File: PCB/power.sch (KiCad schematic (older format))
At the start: 45 parts

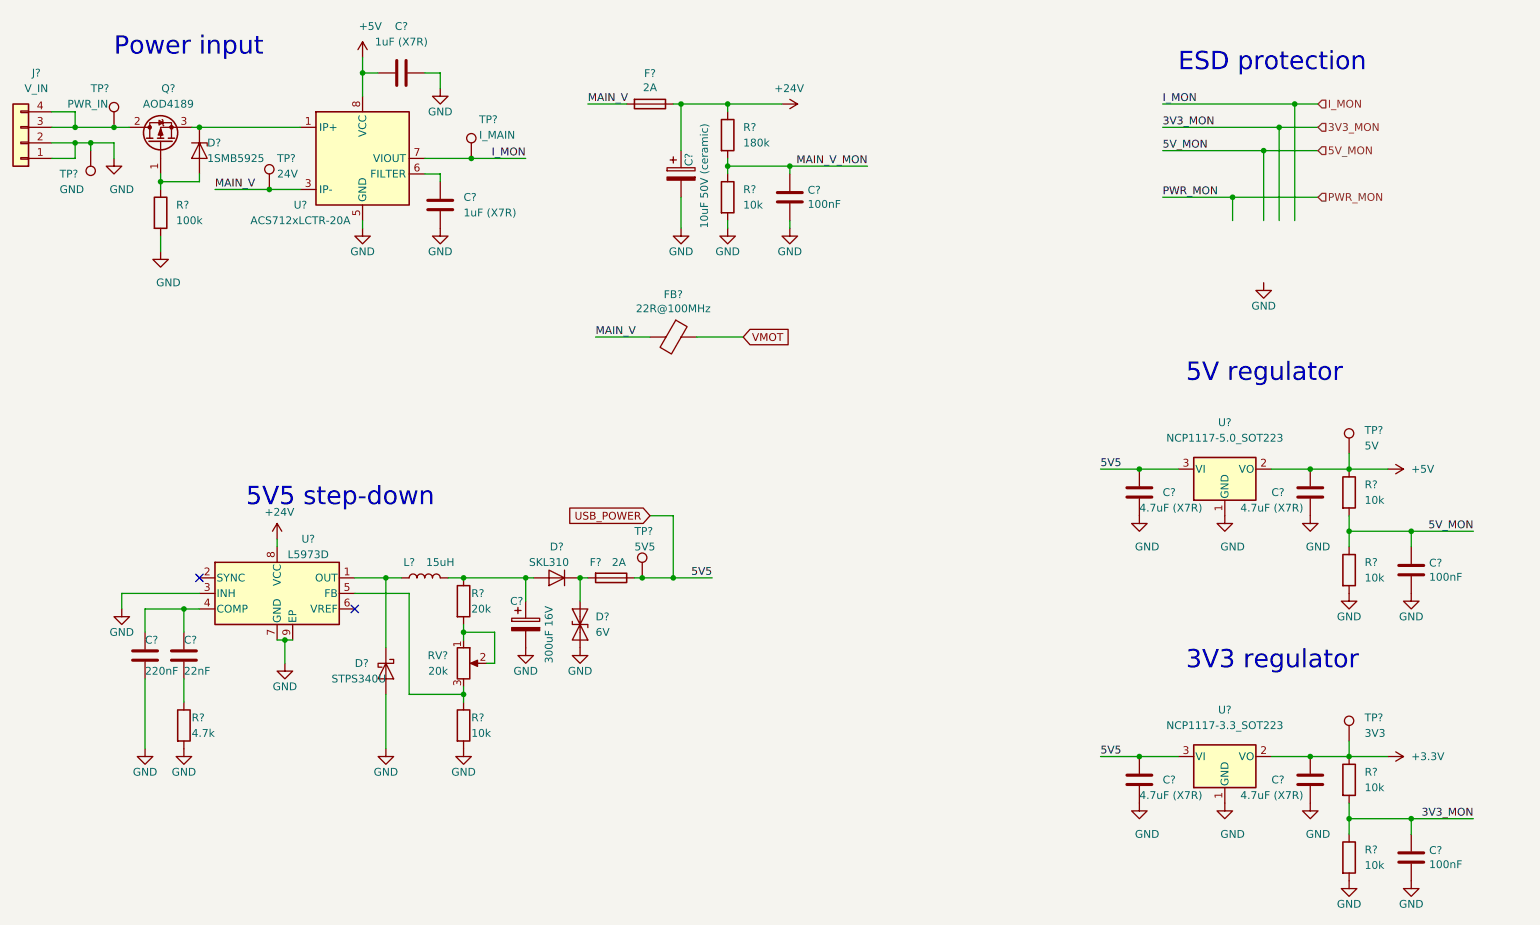
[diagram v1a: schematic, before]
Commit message: Schema: add Interface schema, remove old mcu, add divider to current measuring
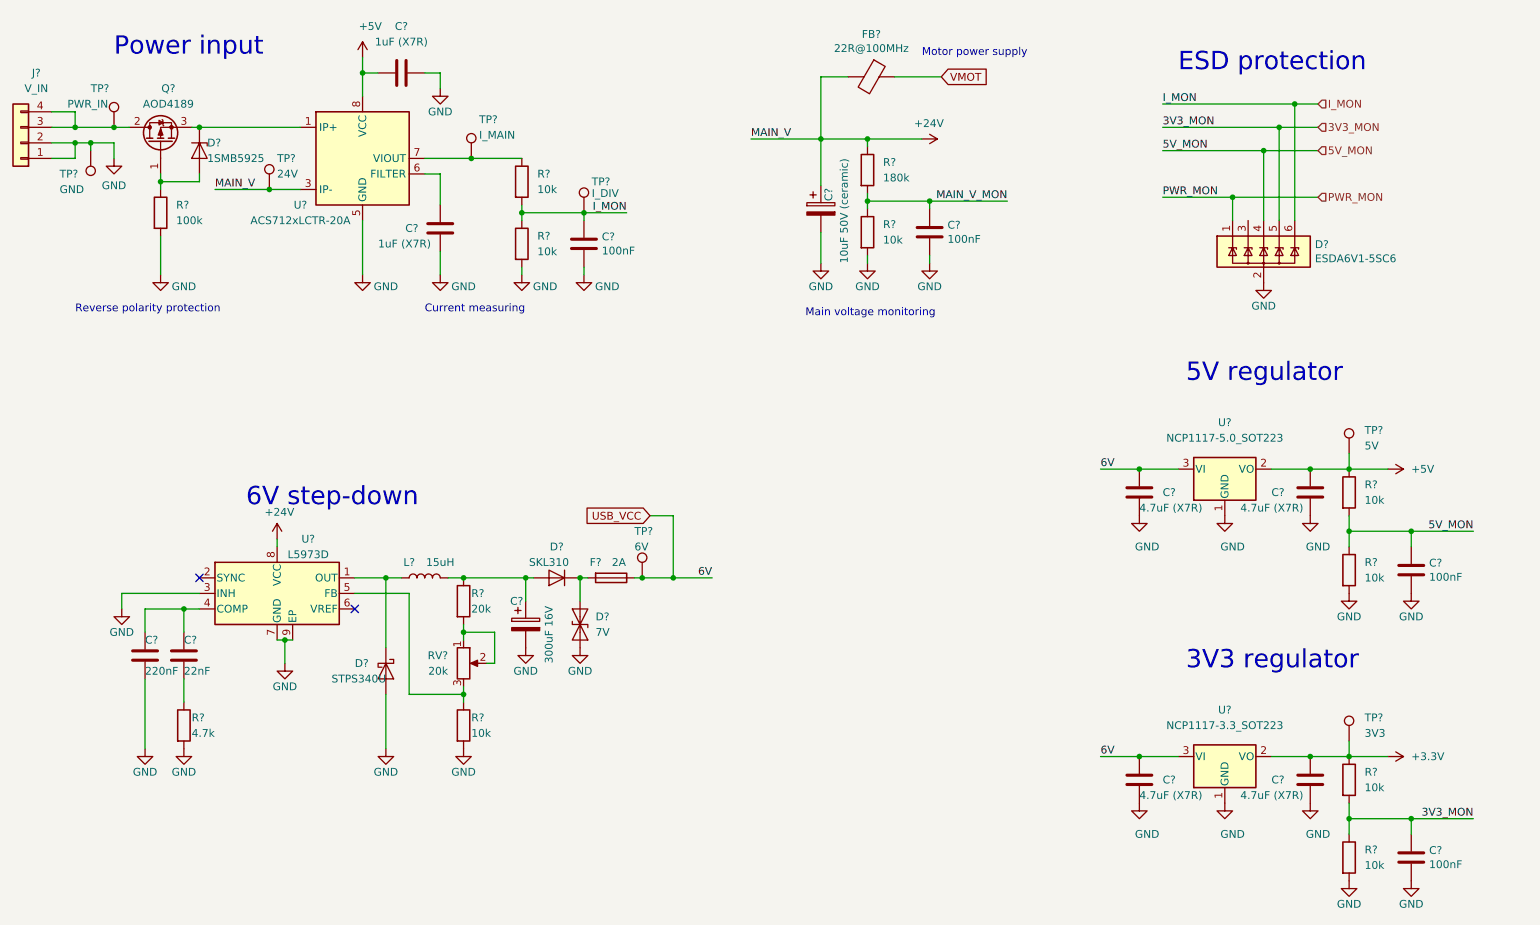
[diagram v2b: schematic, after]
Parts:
- removed F?: 2A, symbol Device:Fuse
- added C?: 100nF, Capacitor_SMD:C_0603_1608Metric, symbol Device:C
- added D?: ESDA6V1-5SC6, Package_TO_SOT_SMD:SOT-23-6, symbol Power_Protection:ESDA6V1-5SC6
- added R? (x2): 10k, Resistor_SMD:R_0603_1608Metric, symbol Device:R
- added TP?: I_DIV, symbol Connector:TestPoint
- D?: value 6V -> 7V
- TP?: value 5V5 -> 6V
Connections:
- net labels added: 6V, USB_VCC
- net labels removed: 5V5, USB_POWER
- wire segments 118 -> 126
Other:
- note added: "6V step-down"
- note added: "Current measuring"
- note added: "Main voltage monitoring"
- note added: "Motor power supply"
- note added: "Reverse polarity protection"
- note removed: "5V5 step-down"
- moved on the sheet: C?, FB?, R?

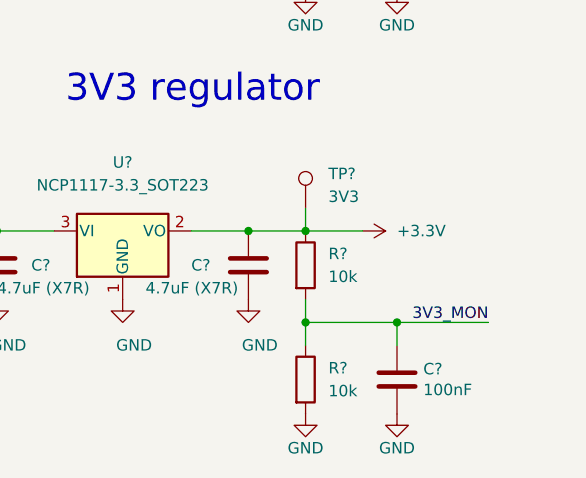
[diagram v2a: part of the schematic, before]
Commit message: Schema: add mcu, RGB LED signalization, reset circuit
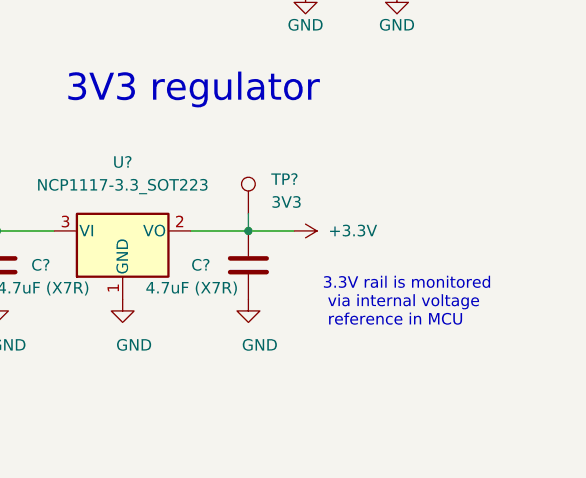
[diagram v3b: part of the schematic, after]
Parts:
- removed C?: 100nF, Capacitor_SMD:C_0603_1608Metric, symbol Device:C
- removed R? (x2): 10k, Resistor_SMD:R_0603_1608Metric, symbol Device:R
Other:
- note added: "3.3V rail is monitored\n via internal voltage\n reference in MCU"
- moved on the sheet: TP?
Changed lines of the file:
@@
-$EndComp
-$Comp
-L Device:R R?
-U 1 1 5CE09E51
-P 9650 5500
-F 0 "R?" H 9750 5550 50  0000 L CNN
-F 1 "10k" H 9750 5450 50  0000 L CNN
-F 2 "Resistor_SMD:R_0603_1608Metric" V 9580 5500 50  0001 C CNN
-F 3 "~" H 9650 5500 50  0001 C CNN
-	1    9650 5500
-	1    0    0    -1
-$EndComp
-$Comp
-L Device:R R?
-U 1 1 5CE09E5B
-P 9650 6000
-F 0 "R?" H 9750 6050 50  0000 L CNN
-F 1 "10k" H 9750 5950 50  0000 L CNN
-F 2 "Resistor_SMD:R_0603_1608Metric" V 9580 6000 50  0001 C CNN
-F 3 "~" H 9650 6000 50  0001 C CNN
-	1    9650 6000
-	1    0    0    -1
-$EndComp
-$Comp
-L power:GND #PWR?
-U 1 1 5CE09E69
-P 9650 6150
-F 0 "#PWR?" H 9650 5900 50  0001 C CNN
-F 1 "GND" H 9650 6000 50  0000 C CNN
-F 2 "" H 9650 6150 50  0001 C CNN
-F 3 "" H 9650 6150 50  0001 C CNN
-	1    9650 6150
-	1    0    0    -1
 $EndComp
 $Comp
 L power:+3.3V #PWR?
 U 1 1 5CE30936
-P 9900 5350
-F 0 "#PWR?" H 9900 5200 50  0001 C CNN
-F 1 "+3.3V" V 9900 5500 50  0000 L CNN
-F 2 "" H 9900 5350 50  0001 C CNN
-F 3 "" H 9900 5350 50  0001 C CNN
-	1    9900 5350
+P 9600 5350
+F 0 "#PWR?" H 9600 5200 50  0001 C CNN
+F 1 "+3.3V" V 9600 5500 50  0000 L CNN
+F 2 "" H 9600 5350 50  0001 C CNN
+F 3 "" H 9600 5350 50  0001 C CNN
+	1    9600 5350
 	0    1    1    0
 $EndComp
-Wire Wire Line
-	9650 5350 9900 5350
 $Comp
 L Device:R R?
@@
 Wire Wire Line
 	9650 3500 9900 3500
-Wire Wire Line
-	9650 5350 9400 5350
-Connection ~ 9650 5350
 Connection ~ 9400 5350
 Wire Wire Line
@@
 L Connector:TestPoint TP?
 U 1 1 5CFEFE42
-P 9650 5250
-F 0 "TP?" H 9750 5400 50  0000 L CNN
-F 1 "3V3" H 9750 5300 50  0000 L CNN
-F 2 "TestPoint:TestPoint_THTPad_D1.5mm_Drill0.7mm" H 9850 5250 50  0001 C CNN
-F 3 "~" H 9850 5250 50  0001 C CNN
-	1    9650 5250
-	1    0    0    -1
-$EndComp
-Wire Wire Line
-	9650 5250 9650 5350
+P 9400 5275
+F 0 "TP?" H 9500 5425 50  0000 L CNN
+F 1 "3V3" H 9500 5325 50  0000 L CNN
+F 2 "TestPoint:TestPoint_THTPad_D1.5mm_Drill0.7mm" H 9600 5275 50  0001 C CNN
+F 3 "~" H 9600 5275 50  0001 C CNN
+	1    9400 5275
+	1    0    0    -1
+$EndComp
 Wire Wire Line
 	5100 4200 5300 4200
@@
 	9200 1300 8450 1300
 Connection ~ 9200 1300
-Wire Wire Line
-	9650 5650 9650 5750
-$Comp
-L Device:C C?
-U 1 1 5D11DA30
-P 10050 6000
-F 0 "C?" H 10165 6046 50  0000 L CNN
-F 1 "100nF" H 10165 5955 50  0000 L CNN
-F 2 "Capacitor_SMD:C_0603_1608Metric" H 10088 5850 50  0001 C CNN
-F 3 "~" H 10050 6000 50  0001 C CNN
-	1    10050 6000
-	1    0    0    -1
-$EndComp
-$Comp
-L power:GND #PWR?
-U 1 1 5D11DA3A
-P 10050 6150
-F 0 "#PWR?" H 10050 5900 50  0001 C CNN
-F 1 "GND" H 10050 6000 50  0000 C CNN
-F 2 "" H 10050 6150 50  0001 C CNN
-F 3 "" H 10050 6150 50  0001 C CNN
-	1    10050 6150
-	1    0    0    -1
-$EndComp
-Wire Wire Line
-	9650 5750 10050 5750
-Connection ~ 10050 5750
-Text Label 10450 5750 2    50   ~ 0
-3V3_MON
-Wire Wire Line
-	10050 5750 10450 5750
-Wire Wire Line
-	10050 5750 10050 5850
-Connection ~ 9650 5750
-Wire Wire Line
-	9650 5750 9650 5850
 Text Label 8450 1300 0    50   ~ 0
 3V3_MON
@@
 Wire Wire Line
 	4325 1850 4725 1850
+Wire Wire Line
+	9400 5275 9400 5350
+Wire Wire Line
+	9400 5350 9600 5350
+Text Notes 9725 5775 0    50   ~ 0
+3.3V rail is monitored\n via internal voltage\n reference in MCU
 $EndSCHEMATC

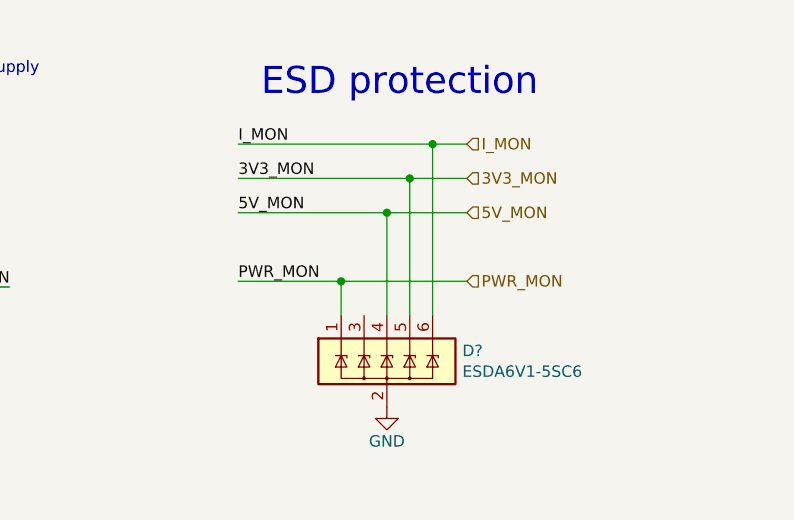
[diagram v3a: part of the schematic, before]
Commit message: Schema: add FLAG and BUSY LED signalization, fix driver ground connection
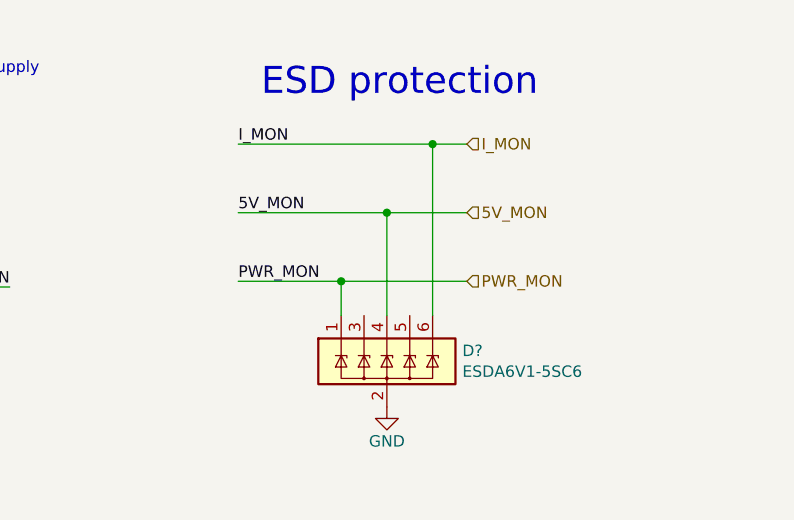
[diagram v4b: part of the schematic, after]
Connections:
- net 3V3_MON: no longer names the net of D?.5 (IO4)
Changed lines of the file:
@@
 Text HLabel 9450 1450 2    50   Input ~ 0
 5V_MON
-Text HLabel 9450 1300 2    50   Input ~ 0
-3V3_MON
 Text HLabel 9450 1750 2    50   Input ~ 0
 PWR_MON
@@
 	9100 1450 9450 1450
 Wire Wire Line
-	9200 1900 9200 1300
-Wire Wire Line
-	9200 1300 9450 1300
-Wire Wire Line
 	8450 1450 9100 1450
 Connection ~ 9100 1450
-Wire Wire Line
-	9200 1300 8450 1300
-Connection ~ 9200 1300
-Text Label 8450 1300 0    50   ~ 0
-3V3_MON
 Text Label 8450 1450 0    50   ~ 0
 5V_MON

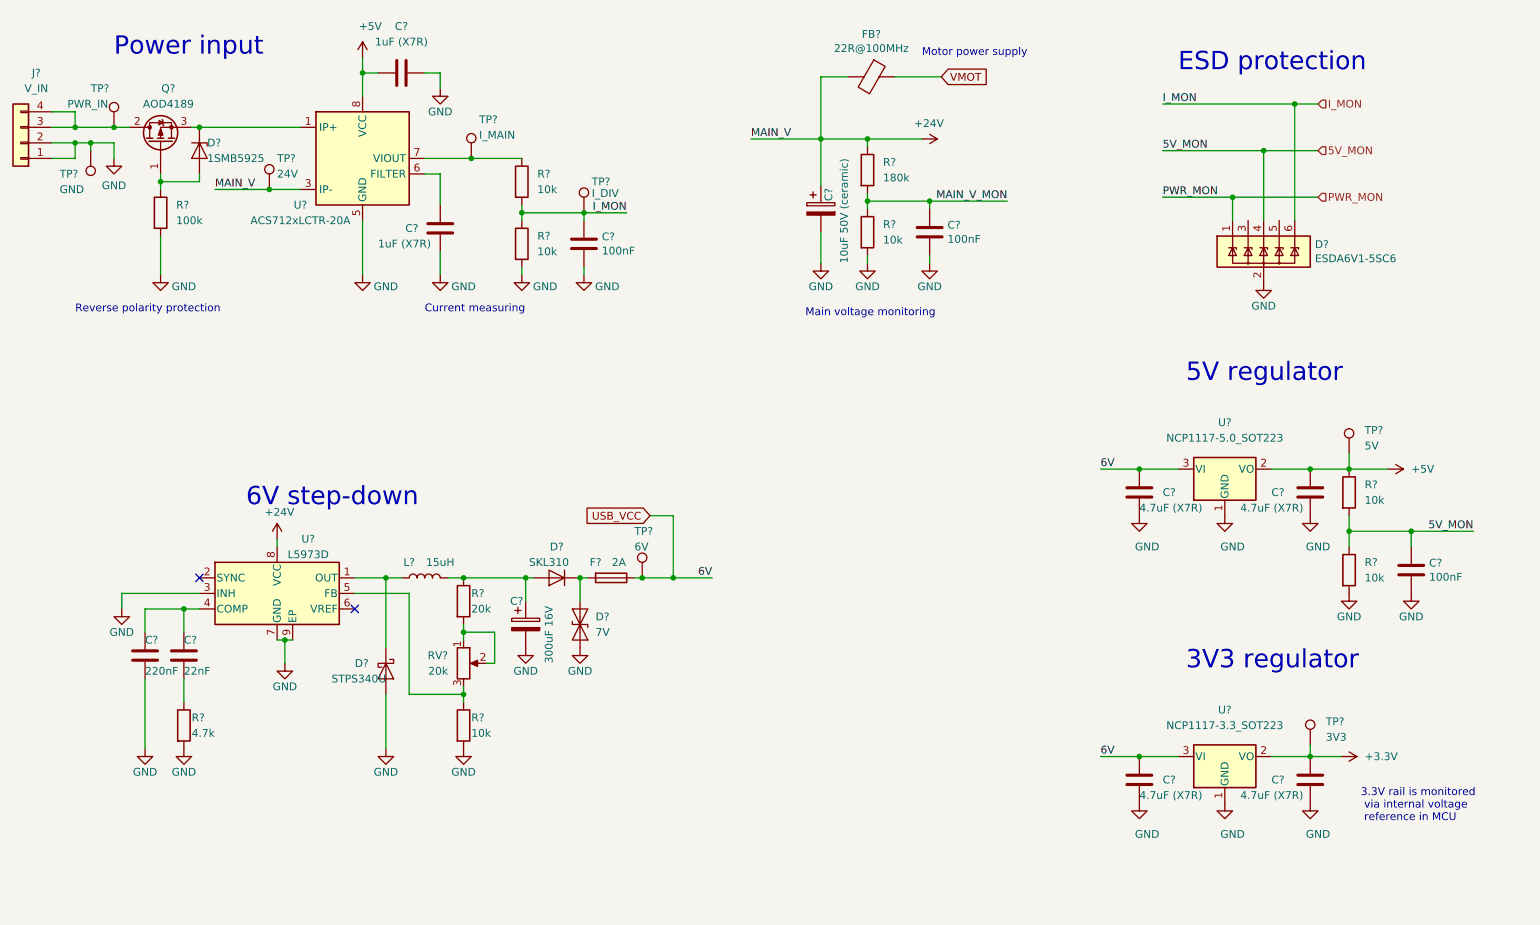
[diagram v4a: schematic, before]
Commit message: Schema: new part annotation, package assignment
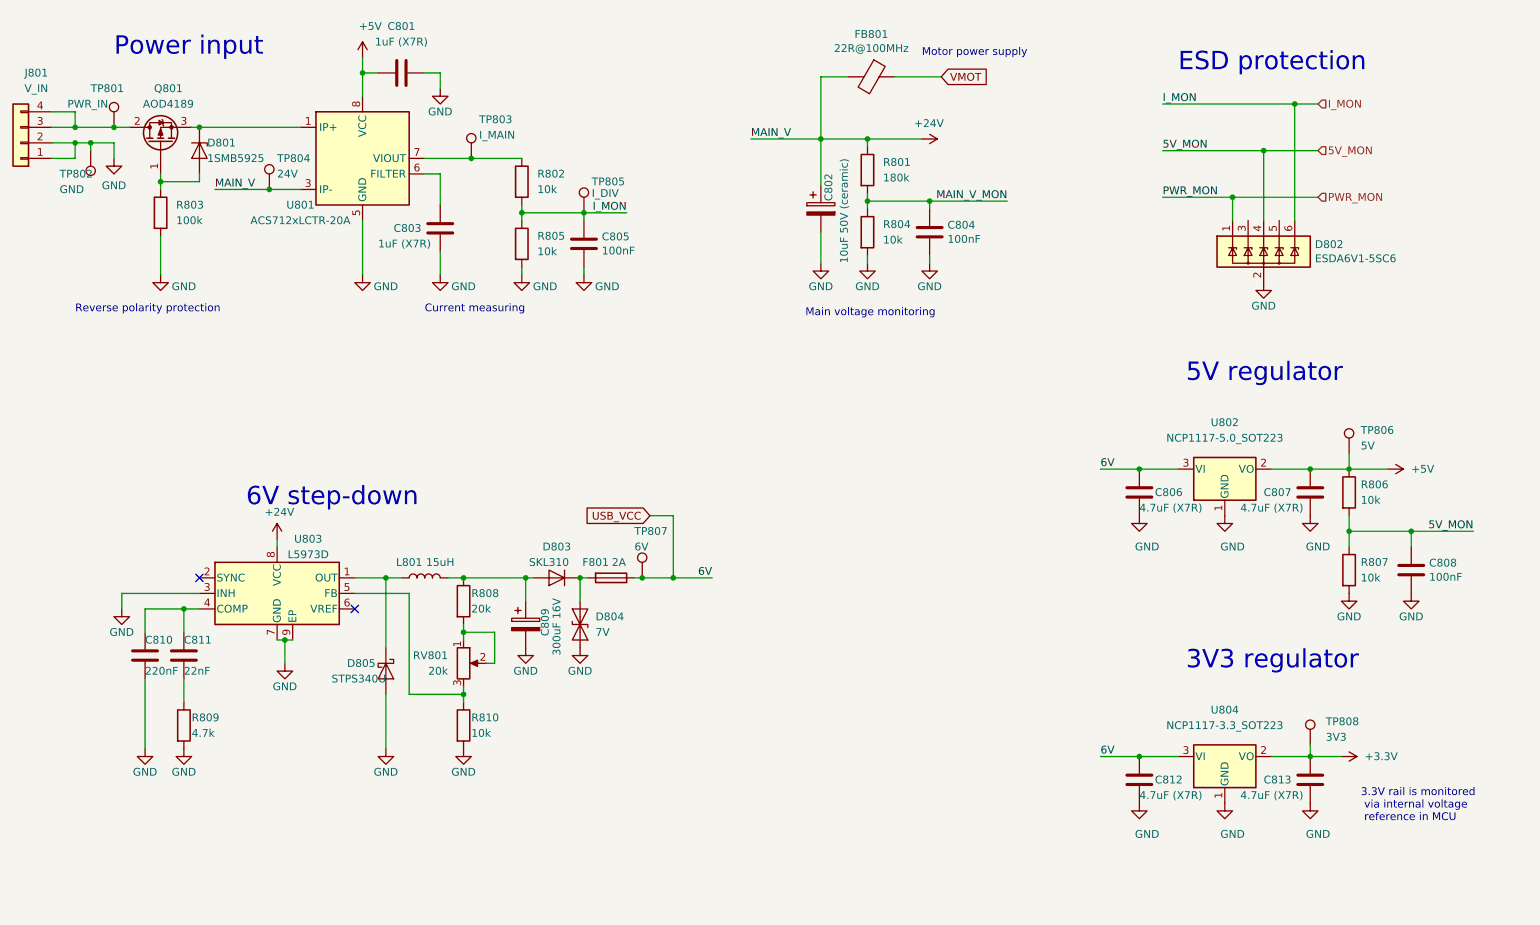
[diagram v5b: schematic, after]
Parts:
- FB801: renamed from FB?; footprint (none) -> Inductor_SMD:L_0805_2012Metric
- TP801, TP802, TP803, TP804, TP806, TP807, TP808: renamed from TP?; footprint TestPoint:TestPoint_THTPad_D1.5mm_Drill0.7mm -> TestPoint:TestPoint_THTPad_D1.0mm_Drill0.5mm
- TP805: renamed from TP?; footprint (none) -> TestPoint:TestPoint_THTPad_D1.0mm_Drill0.5mm
- gave numbers to parts that had none: 37
